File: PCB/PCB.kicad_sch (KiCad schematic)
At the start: 417 parts, among them J2 Conn_OLED_I2C, U1 74AHCT125

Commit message: minor schematic change
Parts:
- A1: footprint Module:RaspberryPi_Pico_Common_Unspecified -> Module:RaspberryPi_Pico_SMD_HandSolder
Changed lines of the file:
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@@
 			)
 		)
-		(property "Footprint" "Module:RaspberryPi_Pico_Common_Unspecified"
+		(property "Footprint" "Module:RaspberryPi_Pico_SMD_HandSolder"
 			(at 370.84 203.2 0)
 			(effects

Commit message: did most of the wiring
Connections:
- net +5V: now also C94.1, D104.4 (VDD)
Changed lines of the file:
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@@
 	)
 	(junction
+		(at 167.64 149.86)
+		(diameter 0)
+		(color 0 0 0 0)
+	)
+	(junction
 		(at 248.92 241.3)
 		(diameter 0)
@@
 					(unit 1)
 				)
+			)
+		)
+	)
+	(symbol
+		(lib_id "power:+5V")
+		(at 167.64 149.86 0)
+		(unit 1)
+		(exclude_from_sim no)
+		(in_bom yes)
+		(on_board yes)
+		(dnp no)
+		(fields_autoplaced yes)
+		(property "Reference" "#PWR0222"
+			(at 167.64 153.67 0)
+			(effects
+				(font
+					(size 1.27 1.27)
+				)
+				(hide yes)
+			)
+		)
+		(property "Value" "+5V"
+			(at 167.64 144.78 0)
+			(effects
+				(font
+					(size 1.27 1.27)
+				)
+			)
+		)
+		(property "Footprint" ""
+			(at 167.64 149.86 0)
+			(effects
+				(font
+					(size 1.27 1.27)
+				)
+				(hide yes)
+			)
+		)
+		(property "Datasheet" ""
+			(at 167.64 149.86 0)
+			(effects
+				(font
+					(size 1.27 1.27)
+				)
+				(hide yes)
+			)
+		)
+		(property "Description" "Power symbol creates a global label with name \"+5V\""
+			(at 167.64 149.86 0)
+			(effects
+				(font
+					(size 1.27 1.27)
+				)
+				(hide yes)
+			)
+		)
+		(pin "1"
+		)
+		(instances
+			(project "PCB"
+				(path "/9eec8c31-e2e7-4ce8-a19c-313dbd6669b7"
+					(reference "#PWR0222")
+					(unit 1)
+				)

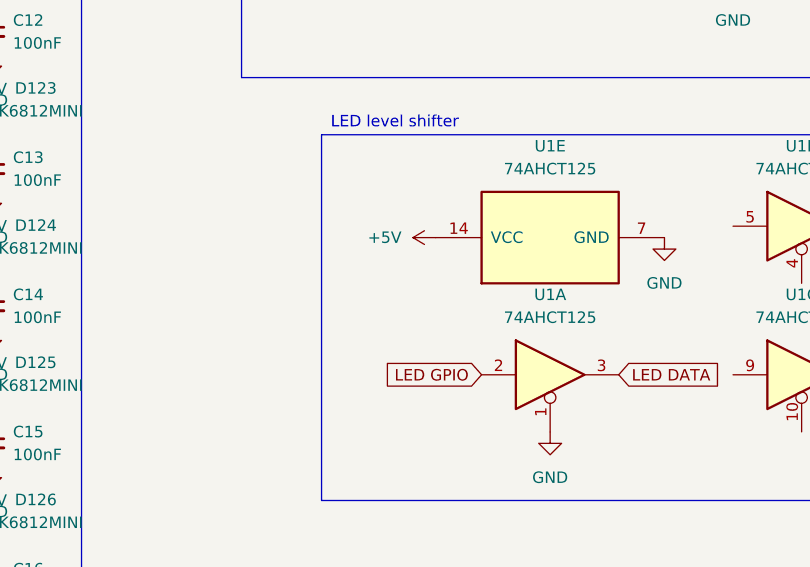
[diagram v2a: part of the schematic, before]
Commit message: added decoupling capacitor near level shifter
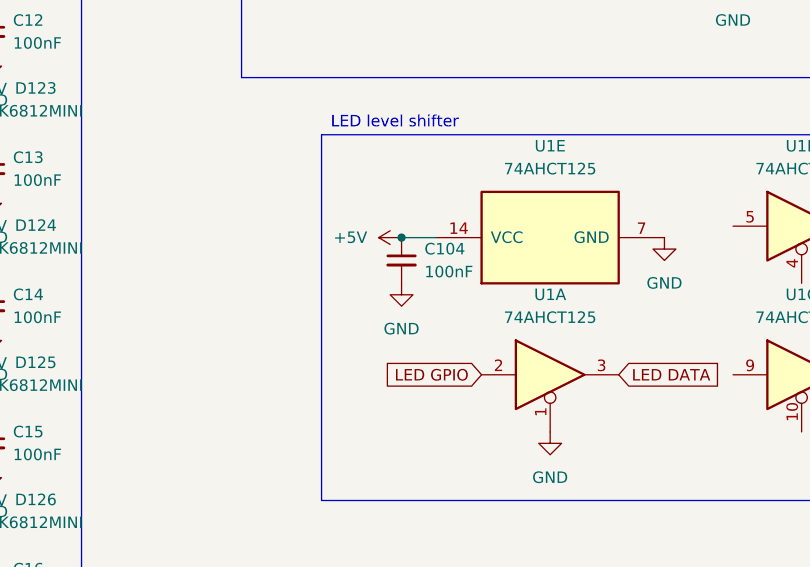
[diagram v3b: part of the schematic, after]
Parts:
- added C104: 100nF, Capacitor_SMD:C_0805_2012Metric_Pad1.18x1.45mm_HandSolder, symbol Device:C_Small
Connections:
- net +5V: now also C104.1
- net GND: now also C104.2
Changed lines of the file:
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@@
 	)
 	(junction
+		(at 334.01 220.98)
+		(diameter 0)
+		(color 0 0 0 0)
+	)
+	(junction
 		(at 95.25 162.56)
 		(diameter 0)
@@
 	(wire
 		(pts
+			(xy 334.01 220.98) (xy 337.82 220.98)
+		)
+		(stroke
+			(width 0)
+			(type default)
+		)
+	)
+	(wire
+		(pts
 			(xy 59.69 181.61) (xy 68.58 181.61)
 		)
@@
 	(symbol
 		(lib_id "power:+5V")
-		(at 337.82 220.98 90)
+		(at 334.01 220.98 90)
 		(unit 1)
 		(exclude_from_sim no)
@@
 		(fields_autoplaced yes)
 		(property "Reference" "#PWR0115"
-			(at 341.63 220.98 0)
+			(at 337.82 220.98 0)
 			(effects
 				(font
@@
 		)
 		(property "Value" "+5V"
-			(at 334.01 220.9799 90)
+			(at 330.2 220.9799 90)
 			(effects
 				(font
@@
 		)
 		(property "Footprint" ""
-			(at 337.82 220.98 0)
+			(at 334.01 220.98 0)
 			(effects
 				(font
@@
 		)
 		(property "Datasheet" ""
-			(at 337.82 220.98 0)
+			(at 334.01 220.98 0)
 			(effects
 				(font
@@
 		)
 		(property "Description" "Power symbol creates a global label with name \"+5V\""
-			(at 337.82 220.98 0)
+			(at 334.01 220.98 0)
 			(effects
 				(font
@@
 	)
 	(symbol
+		(lib_id "power:GND")
+		(at 334.01 226.06 0)
+		(unit 1)
+		(exclude_from_sim no)
+		(in_bom yes)
+		(on_board yes)
+		(dnp no)
+		(fields_autoplaced yes)
+		(property "Reference" "#PWR0223"
+			(at 334.01 232.41 0)
+			(effects
+				(font
+					(size 1.27 1.27)
+				)
+				(hide yes)
+			)
+		)
+		(property "Value" "GND"
+			(at 334.01 231.14 0)
+			(effects
+				(font
+					(size 1.27 1.27)
+				)
+			)
+		)
+		(property "Footprint" ""
+			(at 334.01 226.06 0)
+			(effects
+				(font
+					(size 1.27 1.27)
+				)
+				(hide yes)
+			)
+		)
+		(property "Datasheet" ""
+			(at 334.01 226.06 0)
+			(effects
+				(font
+					(size 1.27 1.27)
+				)
+				(hide yes)
+			)
+		)
+		(property "Description" "Power symbol creates a global label with name \"GND\" , ground"
+			(at 334.01 226.06 0)
+			(effects
+				(font
+					(size 1.27 1.27)
+				)
+				(hide yes)
+			)
+		)
+		(pin "1"
+		)
+		(instances
+			(project "PCB"
+				(path "/9eec8c31-e2e7-4ce8-a19c-313dbd6669b7"
+					(reference "#PWR0223")
+					(unit 1)
+				)
+			)
+		)
+	)
+	(symbol
 		(lib_id "LED:SK6812MINI")
 		(at 232.41 88.9 270)
@@
 					(unit 1)
 				)
+			)
+		)
+	)
+	(symbol
+		(lib_id "Device:C_Small")
+		(at 334.01 223.52 0)
+		(unit 1)
+		(exclude_from_sim no)
+		(in_bom yes)
+		(on_board yes)
+		(dnp no)
+		(fields_autoplaced yes)
+		(property "Reference" "C104"
+			(at 336.55 222.2562 0)
+			(effects
+				(font
+					(size 1.27 1.27)
+				)
+				(justify left)
+			)
+		)
+		(property "Value" "100nF"
+			(at 336.55 224.7962 0)
+			(effects
+				(font
+					(size 1.27 1.27)
+				)
+				(justify left)
+			)
+		)
+		(property "Footprint" "Capacitor_SMD:C_0805_2012Metric_Pad1.18x1.45mm_HandSolder"
+			(at 334.01 223.52 0)
+			(effects
+				(font
+					(size 1.27 1.27)
+				)
+				(hide yes)
+			)
+		)
+		(property "Datasheet" "~"
+			(at 334.01 223.52 0)
+			(effects
+				(font
+					(size 1.27 1.27)
+				)
+				(hide yes)
+			)
+		)
+		(property "Description" "Unpolarized capacitor, small symbol"
+			(at 334.01 223.52 0)
+			(effects
+				(font
+					(size 1.27 1.27)
+				)
+				(hide yes)
+			)
+		)
+		(pin "2"
+		)
+		(pin "1"
+		)
+		(instances
+			(project "PCB"
+				(path "/9eec8c31-e2e7-4ce8-a19c-313dbd6669b7"
+					(reference "C104")
+					(unit 1)
+				)

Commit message: updated the PCB a little bit
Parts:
- added C105: 100nF, Capacitor_SMD:C_0805_2012Metric_Pad1.18x1.45mm_HandSolder, symbol Device:C_Small
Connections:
- net +3V3: now also C105.2
- net GND: now also U1.12, U1.5, U1.9, C105.1

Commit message: updated the case
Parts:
- R1, R2: value 10k -> 4k7
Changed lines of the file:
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@@
 			)
 		)
-		(property "Value" "10k"
+		(property "Value" "4k7"
 			(at 335.28 135.8899 0)
 			(effects
@@
 			)
 		)
-		(property "Value" "10k"
+		(property "Value" "4k7"
 			(at 342.9 135.8899 0)
 			(effects

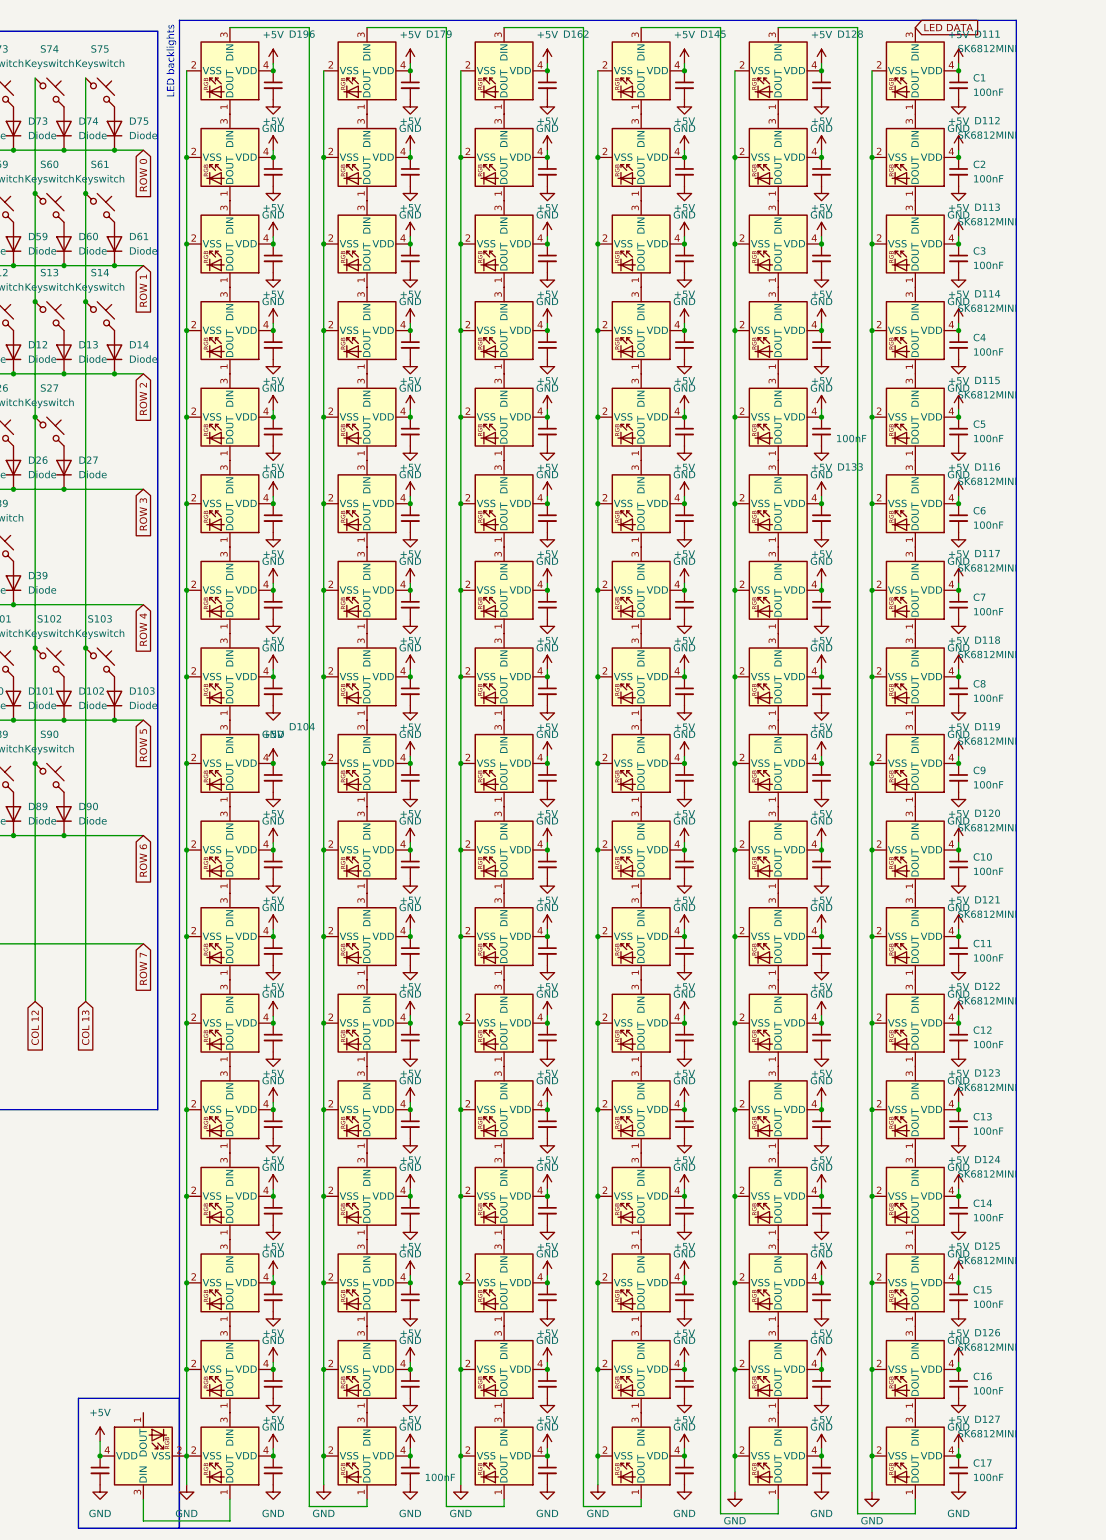
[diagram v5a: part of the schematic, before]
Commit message: remade the NeoPixels on the PCB
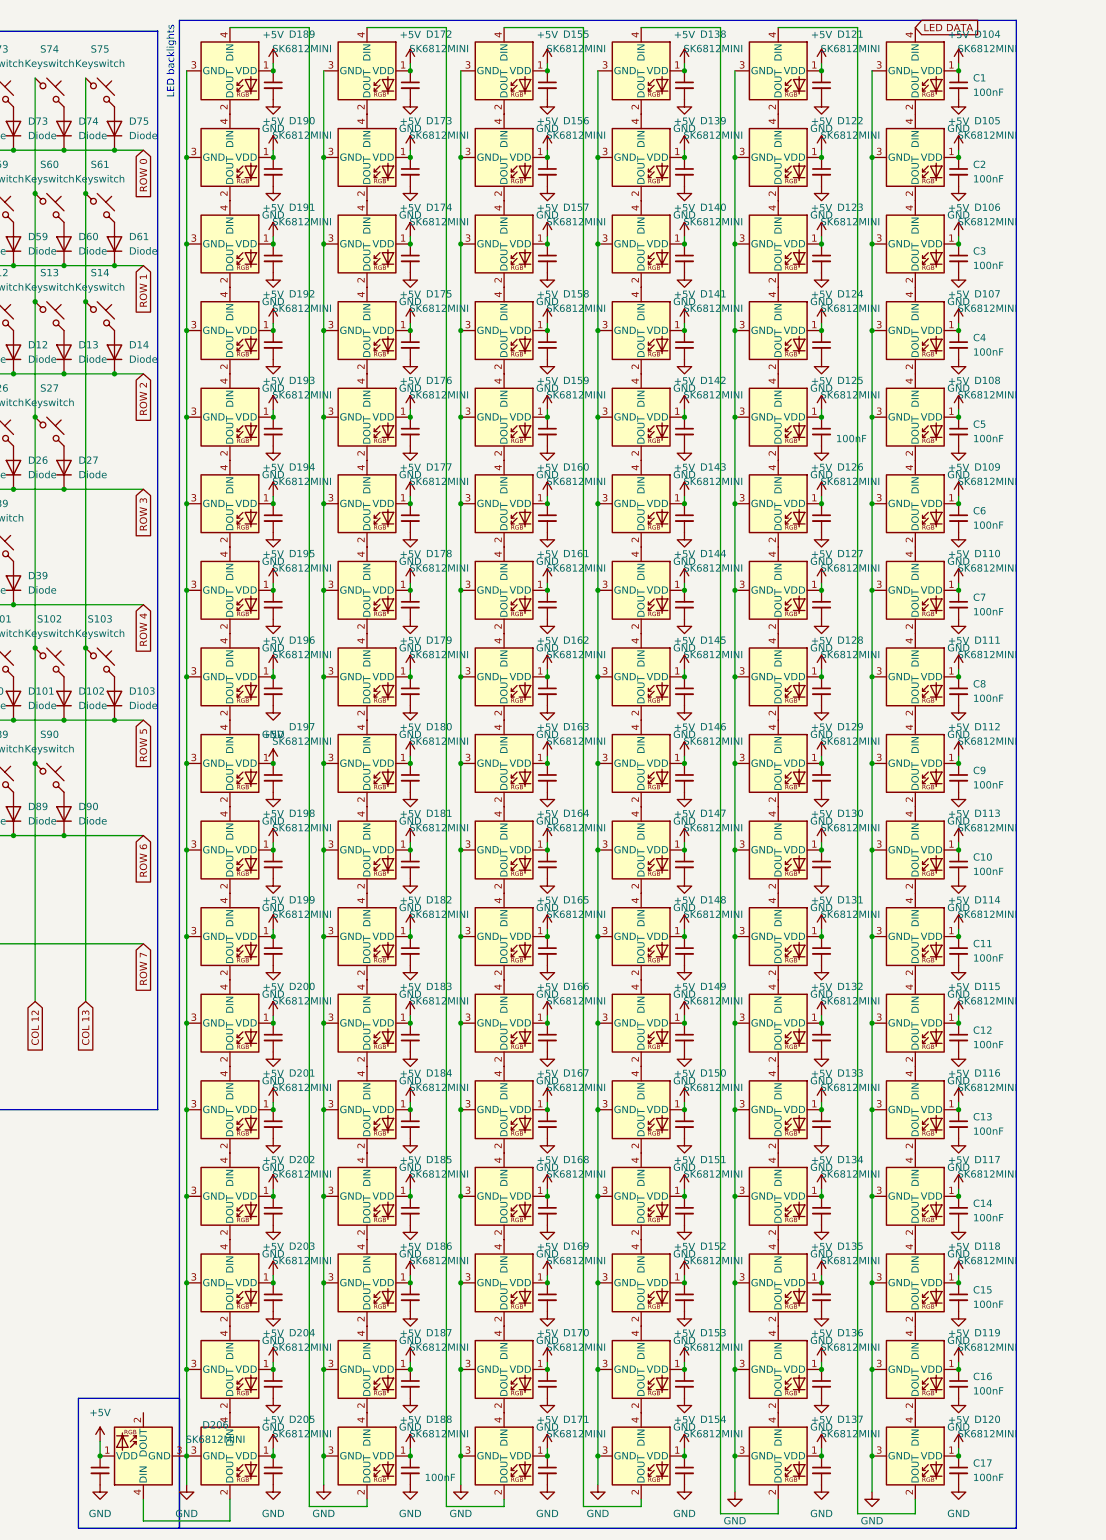
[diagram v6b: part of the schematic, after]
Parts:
- removed D104, D105, D106, D107, D108, D109, D110, D111, D112, D113, D114, D115, D116, D117, D118, D119, D120, D121, D122, D123, D124, D125, D126, D127, D128, D129, D130, D131, D132, D133, D134, D135, D136, D137, D138, D139, D140, D141, D142, D143, D144, D145, D146, D147, D148, D149, D150, D151, D152, D153, D154, D155, D156, D157, D158, D159, D160, D161, D162, D163, D164, D165, D166, D167, D168, D169, D170, D171, D172, D173, D174, D175, D176, D177, D178, D179, D180, D181, D182, D183, D184, D185, D186, D187, D188, D189, D190, D191, D192, D193, D194, D195, D196, D197, D198, D199, D200, D201, D202, D203, D204, D205, D206: SK6812MINI, ScottoKeebs_Components:LED_SK6812MINI, symbol LED:SK6812MINI
- added D104, D105, D106, D107, D108, D109, D110, D111, D112, D113, D114, D115, D116, D117, D118, D119, D120, D121, D122, D123, D124, D125, D126, D127, D128, D129, D130, D131, D132, D133, D134, D135, D136, D137, D138, D139, D140, D141, D142, D143, D144, D145, D146, D147, D148, D149, D150, D151, D152, D153, D154, D155, D156, D157, D158, D159, D160, D161, D162, D163, D164, D165, D166, D167, D168, D169, D170, D171, D172, D173, D174, D175, D176, D177, D178, D179, D180, D181, D182, D183, D184, D185, D186, D187, D188, D189, D190, D191, D192, D193, D194, D195, D196, D197, D198, D199, D200, D201, D202, D203, D204, D205, D206: SK6812MINI, ScottoKeebs_Components:LED_SK6812MINI, symbol WORKING_LED_SK6812:SK6812MINI
- A1: footprint Module:RaspberryPi_Pico_SMD_HandSolder -> Module:RaspberryPi_Pico_Common_Unspecified
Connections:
- net +5V: now also D104.1 (VDD), D105.1 (VDD), D106.1 (VDD), D107.1 (VDD), D108.1 (VDD), D109.1 (VDD), D110.1 (VDD), D111.1 (VDD), D112.1 (VDD), D113.1 (VDD), D114.1 (VDD), D115.1 (VDD), D116.1 (VDD), D117.1 (VDD), D118.1 (VDD), D119.1 (VDD), D120.1 (VDD), D121.1 (VDD), D122.1 (VDD), D123.1 (VDD), D124.1 (VDD), D125.1 (VDD), D126.1 (VDD), D127.1 (VDD), D128.1 (VDD), D129.1 (VDD), D130.1 (VDD), D131.1 (VDD), D132.1 (VDD), D133.1 (VDD), D134.1 (VDD), D135.1 (VDD), D136.1 (VDD), D137.1 (VDD), D138.1 (VDD), D139.1 (VDD), D140.1 (VDD), D141.1 (VDD), D142.1 (VDD), D143.1 (VDD), D144.1 (VDD), D145.1 (VDD), D146.1 (VDD), D147.1 (VDD), D148.1 (VDD), D149.1 (VDD), D150.1 (VDD), D151.1 (VDD), D152.1 (VDD), D153.1 (VDD), D154.1 (VDD), D155.1 (VDD), D156.1 (VDD), D157.1 (VDD), D158.1 (VDD), D159.1 (VDD), D160.1 (VDD), D161.1 (VDD), D162.1 (VDD), D163.1 (VDD), D164.1 (VDD), D165.1 (VDD), D166.1 (VDD), D167.1 (VDD), D168.1 (VDD), D169.1 (VDD), D170.1 (VDD), D171.1 (VDD), D172.1 (VDD), D173.1 (VDD), D174.1 (VDD), D175.1 (VDD), D176.1 (VDD), D177.1 (VDD), D178.1 (VDD), D179.1 (VDD), D180.1 (VDD), D181.1 (VDD), D182.1 (VDD), D183.1 (VDD), D184.1 (VDD), D185.1 (VDD), D186.1 (VDD), D187.1 (VDD), D188.1 (VDD), D189.1 (VDD), D190.1 (VDD), D191.1 (VDD), D192.1 (VDD), D193.1 (VDD), D194.1 (VDD), D195.1 (VDD), D196.1 (VDD), D197.1 (VDD), D198.1 (VDD), D199.1 (VDD), D200.1 (VDD), D201.1 (VDD), D202.1 (VDD), D203.1 (VDD), D204.1 (VDD), D205.1 (VDD), D206.1 (VDD)
- net GND: now also D104.3 (GND), D105.3 (GND), D106.3 (GND), D107.3 (GND), D108.3 (GND), D109.3 (GND), D110.3 (GND), D111.3 (GND), D112.3 (GND), D113.3 (GND), D114.3 (GND), D115.3 (GND), D116.3 (GND), D117.3 (GND), D118.3 (GND), D119.3 (GND), D120.3 (GND), D121.3 (GND), D122.3 (GND), D123.3 (GND), D124.3 (GND), D125.3 (GND), D126.3 (GND), D127.3 (GND), D128.3 (GND), D129.3 (GND), D130.3 (GND), D131.3 (GND), D132.3 (GND), D133.3 (GND), D134.3 (GND), D135.3 (GND), D136.3 (GND), D137.3 (GND), D138.3 (GND), D139.3 (GND), D140.3 (GND), D141.3 (GND), D142.3 (GND), D143.3 (GND), D144.3 (GND), D145.3 (GND), D146.3 (GND), D147.3 (GND), D148.3 (GND), D149.3 (GND), D150.3 (GND), D151.3 (GND), D152.3 (GND), D153.3 (GND), D154.3 (GND), D155.3 (GND), D156.3 (GND), D157.3 (GND), D158.3 (GND), D159.3 (GND), D160.3 (GND), D161.3 (GND), D162.3 (GND), D163.3 (GND), D164.3 (GND), D165.3 (GND), D166.3 (GND), D167.3 (GND), D168.3 (GND), D169.3 (GND), D170.3 (GND), D171.3 (GND), D172.3 (GND), D173.3 (GND), D174.3 (GND), D175.3 (GND), D176.3 (GND), D177.3 (GND), D178.3 (GND), D179.3 (GND), D180.3 (GND), D181.3 (GND), D182.3 (GND), D183.3 (GND), D184.3 (GND), D185.3 (GND), D186.3 (GND), D187.3 (GND), D188.3 (GND), D189.3 (GND), D190.3 (GND), D191.3 (GND), D192.3 (GND), D193.3 (GND), D194.3 (GND), D195.3 (GND), D196.3 (GND), D197.3 (GND), D198.3 (GND), D199.3 (GND), D200.3 (GND), D201.3 (GND), D202.3 (GND), D203.3 (GND), D204.3 (GND), D205.3 (GND), D206.3 (GND)
- net LED DATA: now also D104.4 (DIN)
- new net: D193.2 (DOUT), D194.4 (DIN)
- new net: D192.2 (DOUT), D193.4 (DIN)
- new net: D205.2 (DOUT), D206.4 (DIN)
- new net: D204.2 (DOUT), D205.4 (DIN)
- new net: D106.2 (DOUT), D107.4 (DIN)
- new net: D105.2 (DOUT), D106.4 (DIN)
- new net: D138.2 (DOUT), D139.4 (DIN)
- new net: D137.2 (DOUT), D138.4 (DIN)
- new net: D171.2 (DOUT), D172.4 (DIN)
- new net: D170.2 (DOUT), D171.4 (DIN)
- new net: D181.2 (DOUT), D182.4 (DIN)
- new net: D180.2 (DOUT), D181.4 (DIN)
- new net: D141.2 (DOUT), D142.4 (DIN)
- new net: D140.2 (DOUT), D141.4 (DIN)
- new net: D121.2 (DOUT), D122.4 (DIN)
- new net: D120.2 (DOUT), D121.4 (DIN)
- new net: D152.2 (DOUT), D153.4 (DIN)
- new net: D151.2 (DOUT), D152.4 (DIN)
- new net: D147.2 (DOUT), D148.4 (DIN)
- new net: D146.2 (DOUT), D147.4 (DIN)
- new net: D185.2 (DOUT), D186.4 (DIN)
- new net: D184.2 (DOUT), D185.4 (DIN)
- new net: D125.2 (DOUT), D126.4 (DIN)
- new net: D124.2 (DOUT), D125.4 (DIN)
- new net: D135.2 (DOUT), D136.4 (DIN)
- new net: D134.2 (DOUT), D135.4 (DIN)
- new net: D150.2 (DOUT), D151.4 (DIN)
- new net: D159.2 (DOUT), D160.4 (DIN)
- new net: D158.2 (DOUT), D159.4 (DIN)
- new net: D132.2 (DOUT), D133.4 (DIN)
- new net: D131.2 (DOUT), D132.4 (DIN)
- new net: D202.2 (DOUT), D203.4 (DIN)
- new net: D201.2 (DOUT), D202.4 (DIN)
- new net: D179.2 (DOUT), D180.4 (DIN)
- new net: D199.2 (DOUT), D200.4 (DIN)
- new net: D198.2 (DOUT), D199.4 (DIN)
- new net: D200.2 (DOUT), D201.4 (DIN)
- new net: D122.2 (DOUT), D123.4 (DIN)
- new net: D165.2 (DOUT), D166.4 (DIN)
- new net: D164.2 (DOUT), D165.4 (DIN)
- new net: D149.2 (DOUT), D150.4 (DIN)
- new net: D139.2 (DOUT), D140.4 (DIN)
- new net: D183.2 (DOUT), D184.4 (DIN)
- new net: D182.2 (DOUT), D183.4 (DIN)
- new net: D142.2 (DOUT), D143.4 (DIN)
- new net: D145.2 (DOUT), D146.4 (DIN)
- new net: D143.2 (DOUT), D144.4 (DIN)
- new net: D153.2 (DOUT), D154.4 (DIN)
- new net: D144.2 (DOUT), D145.4 (DIN)
- new net: D178.2 (DOUT), D179.4 (DIN)
- new net: D148.2 (DOUT), D149.4 (DIN)
- new net: D119.2 (DOUT), D120.4 (DIN)
- new net: D160.2 (DOUT), D161.4 (DIN)
- new net: D110.2 (DOUT), D111.4 (DIN)
- new net: D109.2 (DOUT), D110.4 (DIN)
- new net: D190.2 (DOUT), D191.4 (DIN)
- new net: D189.2 (DOUT), D190.4 (DIN)
- new net: D114.2 (DOUT), D115.4 (DIN)
- new net: D113.2 (DOUT), D114.4 (DIN)
- new net: D172.2 (DOUT), D173.4 (DIN)
- new net: D174.2 (DOUT), D175.4 (DIN)
- new net: D173.2 (DOUT), D174.4 (DIN)
- new net: D107.2 (DOUT), D108.4 (DIN)
- new net: D187.2 (DOUT), D188.4 (DIN)
- new net: D186.2 (DOUT), D187.4 (DIN)
- new net: D128.2 (DOUT), D129.4 (DIN)
- new net: D127.2 (DOUT), D128.4 (DIN)
- new net: D203.2 (DOUT), D204.4 (DIN)
- new net: D163.2 (DOUT), D164.4 (DIN)
- new net: D197.2 (DOUT), D198.4 (DIN)
- new net: D123.2 (DOUT), D124.4 (DIN)
- new net: D118.2 (DOUT), D119.4 (DIN)
- new net: D117.2 (DOUT), D118.4 (DIN)
- new net: D108.2 (DOUT), D109.4 (DIN)
- new net: D156.2 (DOUT), D157.4 (DIN)
- new net: D155.2 (DOUT), D156.4 (DIN)
- new net: D177.2 (DOUT), D178.4 (DIN)
- new net: D112.2 (DOUT), D113.4 (DIN)
- new net: D111.2 (DOUT), D112.4 (DIN)
- new net: D191.2 (DOUT), D192.4 (DIN)
- new net: D195.2 (DOUT), D196.4 (DIN)
- new net: D194.2 (DOUT), D195.4 (DIN)
- new net: D154.2 (DOUT), D155.4 (DIN)
- new net: D104.2 (DOUT), D105.4 (DIN)
- new net: D116.2 (DOUT), D117.4 (DIN)
- new net: D115.2 (DOUT), D116.4 (DIN)
- new net: D188.2 (DOUT), D189.4 (DIN)
- new net: D167.2 (DOUT), D168.4 (DIN)
- new net: D166.2 (DOUT), D167.4 (DIN)
- new net: D133.2 (DOUT), D134.4 (DIN)
- new net: D162.2 (DOUT), D163.4 (DIN)
- new net: D196.2 (DOUT), D197.4 (DIN)
- new net: D176.2 (DOUT), D177.4 (DIN)
- new net: D157.2 (DOUT), D158.4 (DIN)
- new net: D169.2 (DOUT), D170.4 (DIN)
- new net: D168.2 (DOUT), D169.4 (DIN)
- new net: D136.2 (DOUT), D137.4 (DIN)
- new net: D126.2 (DOUT), D127.4 (DIN)
- new net: D130.2 (DOUT), D131.4 (DIN)
- new net: D129.2 (DOUT), D130.4 (DIN)
- new net: D175.2 (DOUT), D176.4 (DIN)
- new net: D161.2 (DOUT), D162.4 (DIN)

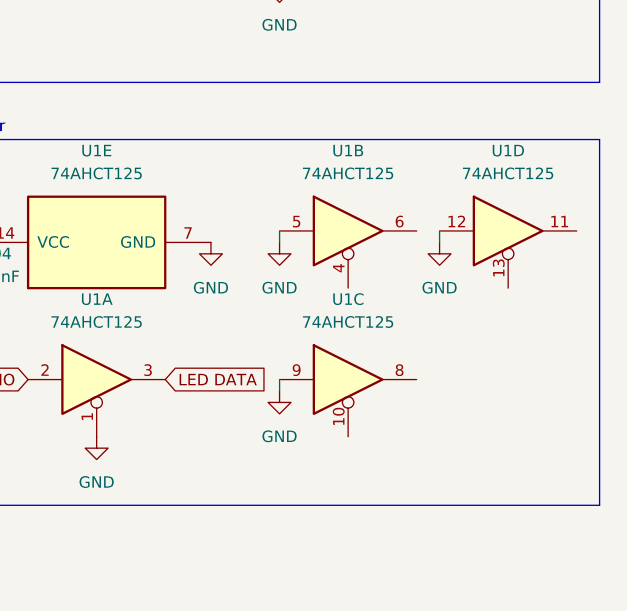
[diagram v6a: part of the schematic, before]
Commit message: Added extra routes for the NeoPixels to even out power distribution
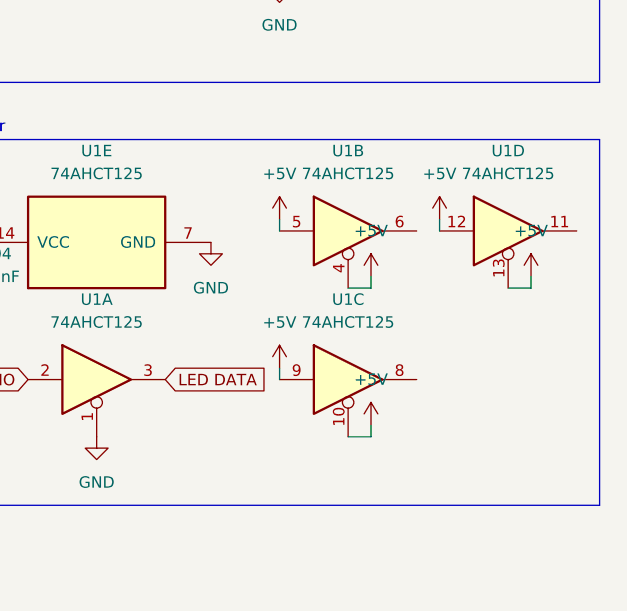
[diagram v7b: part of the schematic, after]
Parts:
- A1: footprint Module:RaspberryPi_Pico_Common_Unspecified -> Module:RaspberryPi_Pico_SMD_HandSolder
- J2: footprint Connector_PinHeader_1.00mm:PinHeader_1x04_P1.00mm_Vertical -> Connector_PinHeader_2.54mm:PinHeader_1x04_P2.54mm_Vertical
- U1: footprint Package_DIP:SMDIP-14_W11.48mm -> Package_SO:SOIC-14_3.9x8.7mm_P1.27mm
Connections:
- net +5V: now also U1.10, U1.12, U1.13, U1.4, U1.5, U1.9
- net GND: no longer U1.12, U1.5, U1.9
